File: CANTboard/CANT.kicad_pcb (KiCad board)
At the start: 2 copper layers, 67.6 x 50.8 mm, 61 parts, among them J1 Conn_02x08_Odd_Even, J2 Screw_Terminal_01x02, J3 Screw_Terminal_01x04, P1 USB, P2 SWD, SW1 SW_SPST, U1 USBLC6-2SC6, U2 SN74LVC1G14DBV, U3 ST485EBDR, U4 LD1117S33TR, U5 STM32H743VITx, U6 MCP2558FD-xSN, U7 74LVC1G66, U8 MCP2558FD-xSN, U9 74LVC1G66, Y1 Crystal

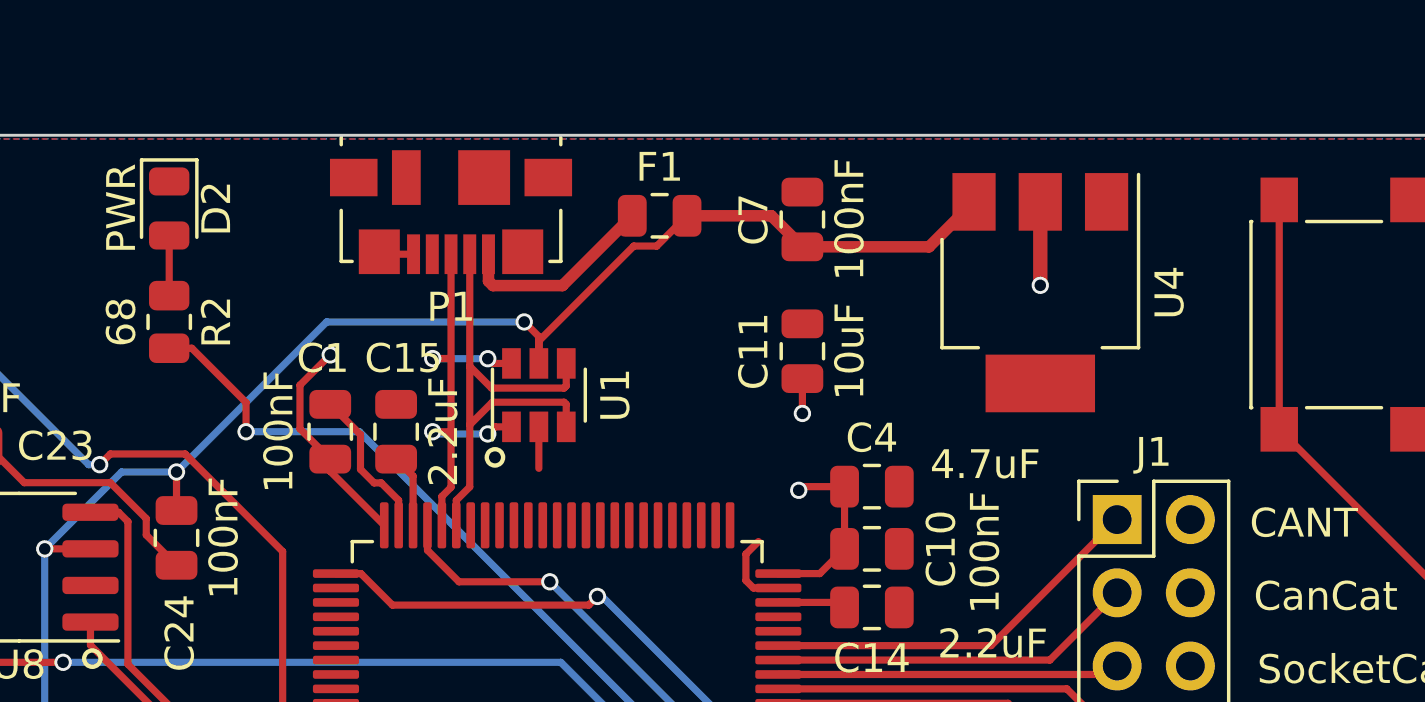
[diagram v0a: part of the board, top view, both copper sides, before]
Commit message: Switched to USB-C, in process of switching to USB-HS
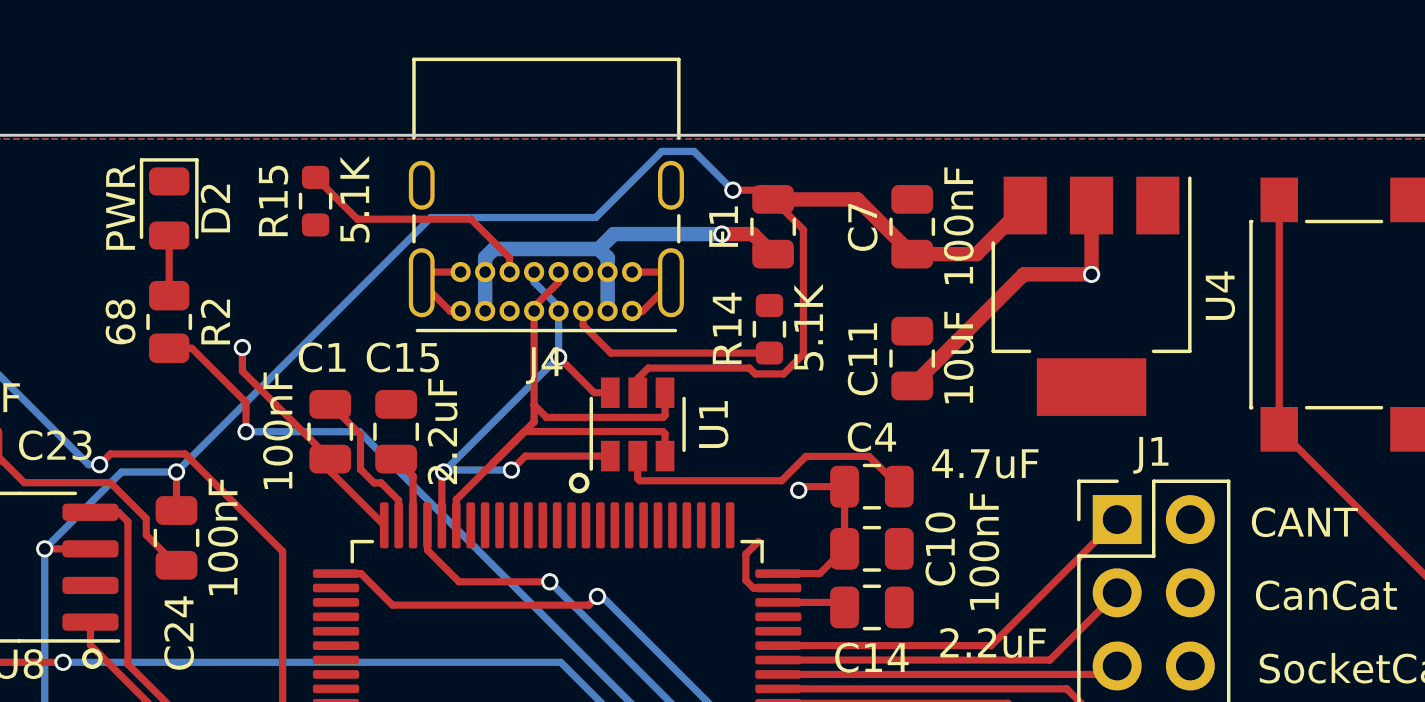
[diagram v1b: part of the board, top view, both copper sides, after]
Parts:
- removed P1: USB, Connector_USB:USB_Micro-B_Molex_47346-0001
- added J4: USB_C_Receptacle_USB2.0, Connector_USB:USB_C_Receptacle_GCT_USB4085, F.Cu at (110.3, 72.5)
- added R14: 5.1K, Resistor_SMD:R_0603_1608Metric, F.Cu at (115.1, 73.2)
- added R15: 5.1K, Resistor_SMD:R_0603_1608Metric, F.Cu at (99.3, 68.7)
- moved F1 3.96 mm to (115.2, 69.6), turned to 90 degrees
- moved C11 3.82 mm to (120.0, 74.2)
- moved C7 3.82 mm to (120.0, 69.6)
- moved U1 3.58 mm to (110.5, 76.5)
- moved U4 1.78 mm to (126.2, 72.0)
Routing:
- net GND: track 117.1 -> 131.6 mm
- net VBUS: track 85.9 -> 100.1 mm
- net Net-(J4-PadB5): track 0.00 -> 8.38 mm
- net Net-(F1-Pad1): track 6.99 -> 14.7 mm, vias 0 -> 1
- net Net-(J4-PadA5): track 0.00 -> 7.36 mm
- net VCC: track 73.8 -> 80.5 mm, vias 15 -> 14
- net /USB_DM: track 18.6 -> 23.0 mm
- net /USB_DP: track 16.5 -> 19.1 mm, vias 4 -> 3
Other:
- board text added: "5.1K"

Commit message: Everything routed, commiting before last check before ordering PCBs
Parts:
- removed P2: SWD, Connector_PinHeader_2.54mm:PinHeader_1x05_P2.54mm_Vertical
- removed Y1: Crystal, Crystal:Crystal_SMD_HC49-SD
- added  : MountingHole_3.2mm_M3, MountingHole:MountingHole_3.2mm_M3, F.Cu at (37.5, 107.3)
- added  : MountingHole_3.2mm_M3, MountingHole:MountingHole_3.2mm_M3, F.Cu at (82.5, 107.3)
- added  : MountingHole_3.2mm_M3, MountingHole:MountingHole_3.2mm_M3, F.Cu at (82.5, 65.4)
- added  : MountingHole_3.2mm_M3, MountingHole:MountingHole_3.2mm_M3, F.Cu at (28.6, 65.4)
- added C25: 100nF, Capacitor_SMD:C_0805_2012Metric, F.Cu at (31.8, 92.7)
- added C26: 1uF, Capacitor_SMD:C_0805_2012Metric, F.Cu at (24.8, 87.6)
- added C27: 1uF, Capacitor_SMD:C_0805_2012Metric, F.Cu at (34.9, 92.7)
- added C28: 100nF, Capacitor_SMD:C_0805_2012Metric, F.Cu at (29.8, 101.0)
- added C29: 100nF, Capacitor_SMD:C_0805_2012Metric, F.Cu at (27.6, 83.2)
- added P1: SWD, Connector_PinHeader_2.54mm:PinHeader_1x05_P2.54mm_Vertical, F.Cu at (66.4, 74.0)
- added R16: 20K, Resistor_SMD:R_0805_2012Metric, F.Cu at (24.8, 91.4)
- added R17: 8.06K, Resistor_SMD:R_0805_2012Metric, F.Cu at (29.2, 92.7)
- added U10: DSC1001, DSC1001:Oscillator_SMD_Microchip_DSC1001-4Pin_2.5x2.0mm, F.Cu at (29.8, 97.8)
- C1: value 100nF -> 1uF
- C11: value 10uF -> 4.7uF
- C12, C13, C14: value 2.2uF -> 100nF
- C15: value 2.2uF -> 1uF
- C16, C17: value 26pF -> 100nF
- C20: value 1uF -> 100nF
- C22, C23, C5: value 100nF -> 2.2uF
- C24: value 100nF -> 4.7uF
- C3: value 100nF -> 10uF
- C4: value 4.7uF -> 2.2uF
- J1: value Conn_02x08_Odd_Even -> USB_C_Receptacle_USB2.0; footprint Connector_PinHeader_2.54mm:PinHeader_2x08_P2.54mm_Vertical -> Connector_USB:USB_C_Receptacle_GCT_USB4085
- J2: value Screw_Terminal_01x02 -> Conn_02x08_Odd_Even; footprint TerminalBlock_Phoenix:TerminalBlock_Phoenix_PT-1,5-2-3.5-H_1x02_P3.50mm_Horizontal -> Connector_PinHeader_2.54mm:PinHeader_2x08_P2.54mm_Vertical
- J4: value USB_C_Receptacle_USB2.0 -> Screw_Terminal_01x02; footprint Connector_USB:USB_C_Receptacle_GCT_USB4085 -> TerminalBlock_Phoenix:TerminalBlock_Phoenix_PT-1,5-2-3.5-H_1x02_P3.50mm_Horizontal
- R1, R2: value 68 -> 5.1K
- R11: value 120 -> 4.7K
- R13: value 10k -> 4.7K
- R14, R15: value 5.1K -> 47; footprint Resistor_SMD:R_0603_1608Metric -> Resistor_SMD:R_0805_2012Metric
- R4, R5: value 4.7K -> 68
- R7: value 47 -> 10k
- R8: value 47 -> 120
- U1: value USBLC6-2SC6 -> USB3343; footprint Package_TO_SOT_SMD:SOT-23-6 -> Package_DFN_QFN:QFN-24-1EP_4x4mm_P0.5mm_EP2.6x2.6mm
- U2: value SN74LVC1G14DBV -> LD1117S33TR; footprint Package_TO_SOT_SMD:SOT-23-5 -> Package_TO_SOT_SMD:SOT-223
- U3: value ST485EBDR -> STM32H743VITx; footprint Package_SO:SOIC-8_3.9x4.9mm_P1.27mm -> Package_QFP:LQFP-100_14x14mm_P0.5mm
- U4: value LD1117S33TR -> MCP2558FD-xSN; footprint Package_TO_SOT_SMD:SOT-223 -> Package_SO:SOIC-8_3.9x4.9mm_P1.27mm
- U5: value STM32H743VITx -> MCP2558FD-xSN; footprint Package_QFP:LQFP-100_14x14mm_P0.5mm -> Package_SO:SOIC-8_3.9x4.9mm_P1.27mm
- U6: value MCP2558FD-xSN -> 74LVC1G66; footprint Package_SO:SOIC-8_3.9x4.9mm_P1.27mm -> Package_TO_SOT_SMD:SOT-353_SC-70-5_Handsoldering
- U8: value MCP2558FD-xSN -> SN74LVC1G14DBV; footprint Package_SO:SOIC-8_3.9x4.9mm_P1.27mm -> Package_TO_SOT_SMD:SOT-23-5
- U9: value 74LVC1G66 -> ST485EBDR; footprint Package_TO_SOT_SMD:SOT-353_SC-70-5_Handsoldering -> Package_SO:SOIC-8_3.9x4.9mm_P1.27mm
- moved SW1 117.1 mm to (22.2, 104.1), turned to 0 degrees
- moved U2 110.0 mm to (19.1, 69.8), turned to 90 degrees
- moved J1 106.2 mm to (21.0, 83.8), turned to 270 degrees
- moved R6 101.4 mm to (28.6, 105.7), turned to 270 degrees
- moved C2 98.0 mm to (25.4, 73.0), turned to 0 degrees
- moved F1 94.0 mm to (21.6, 78.1), turned to 270 degrees
- moved R13 90.4 mm to (45.1, 67.9), turned to 180 degrees
- moved C8 87.9 mm to (40.6, 87.0)
- moved C1 83.3 mm to (16.5, 78.1), turned to 270 degrees
- moved G*** 82.4 mm to (33.0, 85.7)
- moved C14 81.0 mm to (39.1, 97.8)
- moved C7 80.8 mm to (40.6, 84.5), turned to 0 degrees
- moved R14 80.5 mm to (34.5, 71.1)
- moved C3 80.3 mm to (25.4, 69.2), turned to 0 degrees
- moved U1 80.1 mm to (31.1, 87.0), turned to 180 degrees
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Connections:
- C1 pad 1: VCC -> GND
- C1 pad 2: GND -> Net-(C1-Pad2)
- C10 pad 1: VCC -> GND
- C10 pad 2: GND -> VCC
- C11 pad 1: VCC -> GND
- C11 pad 2: GND -> VCC
- C12 pad 1: Net-(C12-Pad1) -> GND
- C12 pad 2: GND -> VCC
- C13 pad 2: Net-(C13-Pad2) -> VCC
- C14 pad 1: Net-(C14-Pad1) -> GND
- C14 pad 2: GND -> VCC
- C15 pad 1: Net-(C15-Pad1) -> GND
- C15 pad 2: GND -> VCC
- C16 pad 1: GND -> VCC
- C16 pad 2: Net-(C16-Pad2) -> GND
- C17 pad 1: Net-(C17-Pad1) -> GND
- C17 pad 2: GND -> VBUS
- C18 pad 1: GND -> VCC
- C18 pad 2: /NRST -> GND
- C19 pad 2: VCC -> VBUS
- C2 pad 1: GND -> VBUS
- C2 pad 2: VCC -> GND
- C22 pad 1: GND -> Net-(C22-Pad1)
- C22 pad 2: VBUS -> GND
- C23 pad 2: VCC -> Net-(C23-Pad2)
- C4 pad 1: VCC -> Net-(C4-Pad1)
- C5 pad 1: VCC -> Net-(C5-Pad1)
- C6 pad 1: VCC -> GND
- C6 pad 2: GND -> /Microcontroller/NRST
- C7 pad 1: VBUS -> GND
- C7 pad 2: GND -> VCC
- C8 pad 1: VCC -> GND
- C8 pad 2: GND -> VCC
- C9 pad 1: VCC -> GND
- C9 pad 2: GND -> VCC
- F1 pad 1: Net-(F1-Pad1) -> VBUS
- F1 pad 2: VBUS -> Net-(F1-Pad2)
- J2 pad 2: Net-(J2-Pad2) -> VCC
- J3 pad 1: CAN1_L -> CAN3_L
- J3 pad 2: CAN1_H -> CAN3_H
- J3 pad 3: CAN2_L -> CAN1_L
- J3 pad 4: CAN2_H -> CAN1_H
- JP1 pad 1: Net-(JP1-Pad1) -> (no net)
- JP1 pad 2: CAN2_L -> BOOT0
- JP1 pad 3: Net-(JP1-Pad3) -> VCC
- JP2 pad 1: Net-(JP2-Pad1) -> (no net)
- JP2 pad 2: CAN1_L -> CAN3_L
- JP3 pad 1: Net-(JP3-Pad1) -> (no net)
- JP3 pad 2: BOOT0 -> CAN1_L
- JP3 pad 3: VCC -> Net-(JP3-Pad3)
- R1 pad 1: Net-(D1-Pad2) -> GND
- R1 pad 2: LED_ACT1 -> Net-(J1-PadA5)
- R10 pad 1: CAN2_SHORT -> CAN3_SHORT
- R11 pad 1: Net-(JP2-Pad3) -> CAN1_SHORT
- R11 pad 2: CAN1_H -> GND
- R12 pad 1: CAN1_SHORT -> Net-(C22-Pad1)
- R13 pad 1: BOOT0 -> VBUS
- R13 pad 2: GND -> Net-(C23-Pad2)
- R14 pad 1: Net-(J4-PadA5) -> Net-(C22-Pad1)
- R14 pad 2: GND -> Net-(J4-Pad2)
- R15 pad 1: GND -> Net-(C23-Pad2)
- R15 pad 2: Net-(J4-PadB5) -> Net-(J4-Pad1)
- R2 pad 1: Net-(D2-Pad2) -> GND
- R2 pad 2: LED_PWR1 -> Net-(J1-PadB5)
- R3 pad 1: Net-(D3-Pad2) -> Net-(D1-Pad2)
- R3 pad 2: LED_ACT2 -> LED_ACT1
- R4 pad 1: Net-(C12-Pad1) -> Net-(D2-Pad2)
- R4 pad 2: GND -> LED_PWR1
- R5 pad 1: VBUS -> Net-(D3-Pad2)
- R5 pad 2: Net-(C13-Pad2) -> LED_ACT2
- R6 pad 2: /NRST -> /Microcontroller/NRST
- R7 pad 1: Net-(C12-Pad1) -> BOOT0
- R7 pad 2: Net-(J2-Pad2) -> GND
- R8 pad 1: Net-(C13-Pad2) -> Net-(JP2-Pad3)
- R8 pad 2: Net-(J2-Pad1) -> CAN3_H
- R9 pad 1: Net-(JP1-Pad3) -> Net-(JP3-Pad3)
- R9 pad 2: CAN2_H -> CAN1_H
- SW1 pad 2: /NRST -> /Microcontroller/NRST
- U1 pad 1: /USB_DP -> USB_DIR
- U1 pad 2: GND -> USB_CK
- U1 pad 3: /USB_DM -> USB_NXT
- U1 pad 4: /USB_DM -> USB_D0
- U1 pad 5: VBUS -> USB_D1
- U1 pad 6: /USB_DP -> USB_D2
- U2 pad 1: Net-(U2-Pad1) -> GND
- U2 pad 2: J1708_TX -> VCC
- U2 pad 3: GND -> VBUS
- U2 pad 4: Net-(U2-Pad4) -> (no net)
- U3 pad 1: J1708_RX -> (no net)
- U3 pad 2: GND -> (no net)
- U3 pad 3: Net-(U2-Pad4) -> (no net)
- U3 pad 4: GND -> (no net)
- U3 pad 5: GND -> (no net)
- U3 pad 6: Net-(C13-Pad2) -> VCC
- U3 pad 7: Net-(C12-Pad1) -> (no net)
- U3 pad 8: VCC -> (no net)
- U4 pad 1: GND -> CAN3_TX
- U4 pad 2: VCC -> GND
- U4 pad 4: (no net) -> CAN3_RX
- U5 pad 1: Net-(U5-Pad1) -> CAN1_TX
- U5 pad 2: Net-(U5-Pad2) -> GND
- U5 pad 3: Net-(U5-Pad3) -> VBUS
- U5 pad 4: Net-(U5-Pad4) -> CAN1_RX
- U5 pad 5: Net-(U5-Pad5) -> VCC
- U5 pad 6: VCC -> CAN1_L
- U5 pad 7: Net-(U5-Pad7) -> CAN1_H
- U5 pad 8: Net-(U5-Pad8) -> GND
- U6 pad 1: CAN2_TX -> CAN3_L
- U6 pad 2: GND -> CAN3_H
- U6 pad 3: VBUS -> GND
- U6 pad 4: CAN2_RX -> CAN3_SHORT
- U7 pad 1: CAN2_L -> CAN1_L
- U7 pad 2: CAN2_H -> CAN1_H
- U7 pad 4: CAN2_SHORT -> CAN1_SHORT
- U8 pad 1: CAN1_TX -> (no net)
- U8 pad 2: GND -> J1708_TX
- U8 pad 3: VBUS -> GND
- U8 pad 4: CAN1_RX -> Net-(U8-Pad4)
- U9 pad 1: CAN1_L -> J1708_RX
- U9 pad 2: CAN1_H -> GND
- U9 pad 3: GND -> Net-(U8-Pad4)
- U9 pad 4: CAN1_SHORT -> GND
- U9 pad 5: VCC -> GND
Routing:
- net /NRST: track 99.4 -> 0.00 mm, vias 1 -> 0
- net /Microcontroller/NRST: track 0.00 -> 80.9 mm, vias 0 -> 4
- net /SWDIO: track 48.1 -> 0.00 mm, vias 1 -> 0
- net /SWCLK: track 47.9 -> 0.00 mm, vias 1 -> 0
- net CAN3_H: track 0.00 -> 47.7 mm
- net CAN2_L: track 39.8 -> 0.00 mm, vias 2 -> 0
- net USB_D7: track 0.00 -> 38.6 mm, vias 0 -> 2
- net CAN3_SHORT: track 0.00 -> 38.6 mm, vias 0 -> 2
- net USB_D6: track 0.00 -> 36.8 mm, vias 0 -> 2
- net USB_STP: track 0.00 -> 36.4 mm, vias 0 -> 2
- net USB_D5: track 0.00 -> 36.1 mm, vias 0 -> 2
- net CAN2_SHORT: track 35.7 -> 0.00 mm, vias 2 -> 0
- net USB_D2: track 0.00 -> 35.7 mm, vias 0 -> 2
- net USB_D3: track 0.00 -> 35.6 mm, vias 0 -> 2
- net USB_DIR: track 0.00 -> 35.5 mm, vias 0 -> 2
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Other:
- board size 67.6 x 50.8 mm -> 82 x 49.1 mm
- copper layers 2 -> 4
- board text added: "1. CanCat 2. CANT 3. SocketCan 4. TruckDevil"
- board text added: "8 7 6 5 4 3 2 1"
- board text added: "CAN 1 - +"
- board text added: "CAN 2 - +"
- board text added: "RST"
- board text added: "SWCLK"
- board text added: "SWDIO"
- board text added: "Term"
- board text removed: "100K"
- board text removed: "100nF"
- board text removed: "10K"
- board text removed: "10uF"
- board text removed: "120"
- board text removed: "1uF"
- board text removed: "2.2uF"
- board text removed: "26pF"
- board text removed: "4.7K"
- board text removed: "4.7uF"
- board text removed: "47"
- board text removed: "5.1K"
- board text removed: "68"
- board text removed: "CAN1"
- board text removed: "CAN2"
- board text removed: "CANT"
- board text removed: "CLK"
- board text removed: "CanCat"
- board text removed: "DIO"
- board text removed: "HI"
- board text removed: "J1708"
- board text removed: "LO"
- board text removed: "NRST"
- board text removed: "PWR"
- board text removed: "Prog1"
- board text removed: "Prog2"
- board text removed: "Prog3"
- board text removed: "Prog4"
- board text removed: "SWD"
- board text removed: "SocketCan"
- board text removed: "TERM"
- board text removed: "TruckDevil"

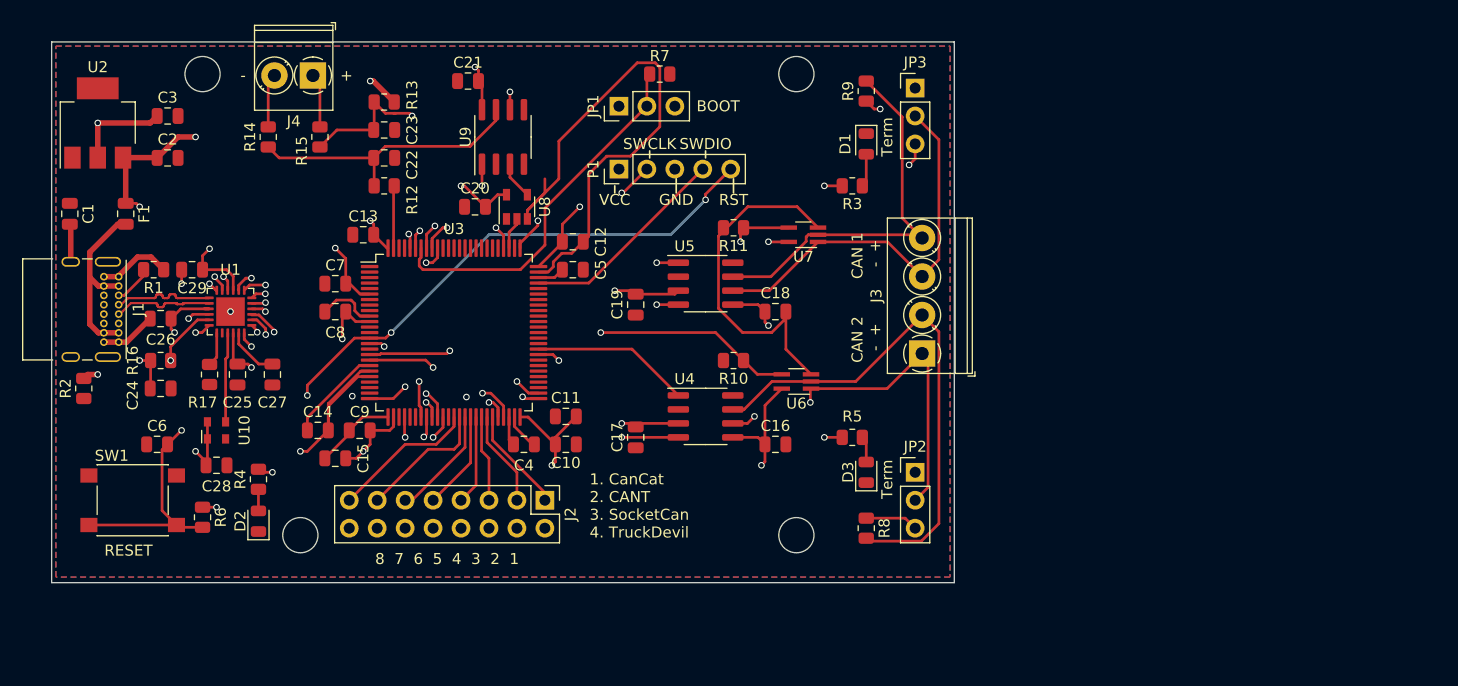
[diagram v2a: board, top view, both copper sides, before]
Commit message: Final review, ordering v0.1 PCB off this design
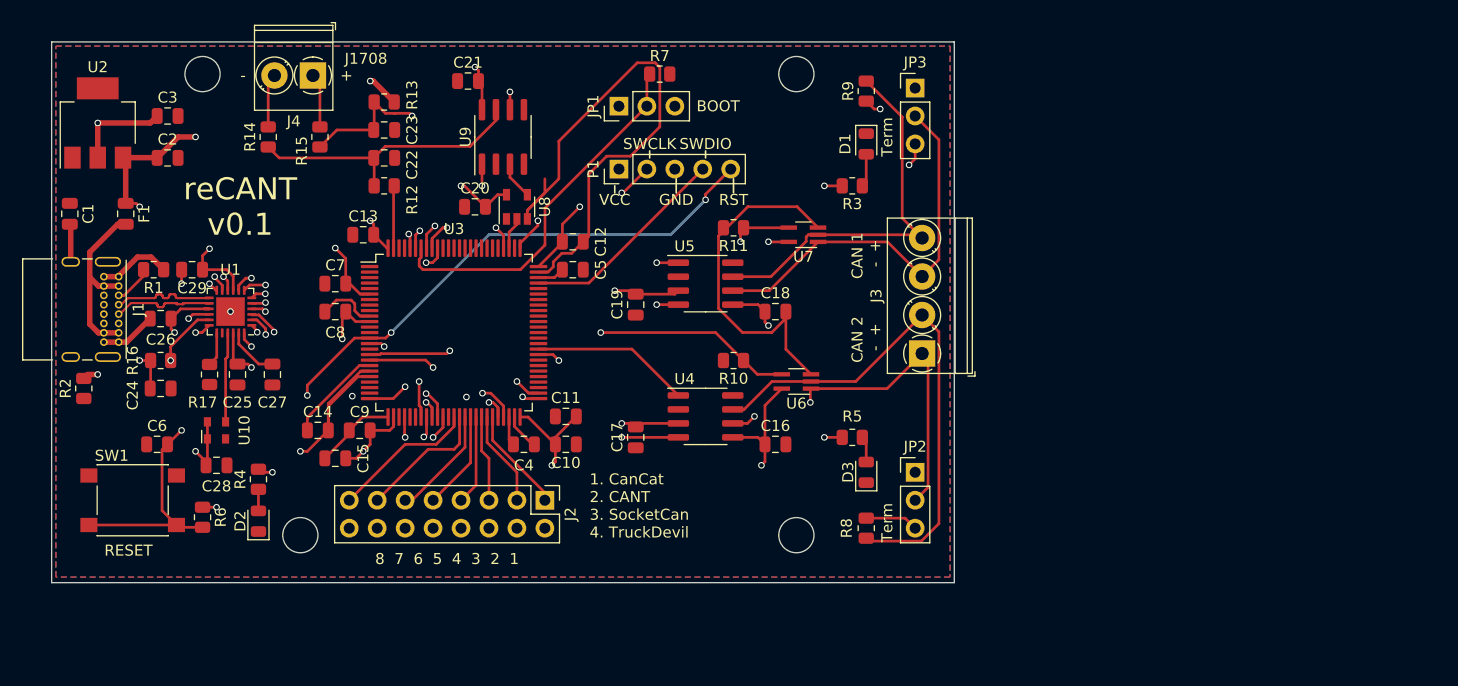
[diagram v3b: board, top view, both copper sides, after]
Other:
- board text added: "J1708"
- board text added: "reCANT v0.1"
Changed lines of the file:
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@@
   (general
     (thickness 1.6)
-    (drawings 25)
+    (drawings 27)
     (tracks 3009)
     (zones 0)
@@
     (tags resistor)
     (attr smd)
-    (fp_text reference R8 (at 0 -1.65 90) (layer F.SilkS)
+    (fp_text reference R8 (at 0 1.778 90) (layer F.SilkS)
       (effects (font (size 1 1) (thickness 0.15)))
     )
@@
     )
   )
+  (gr_text J1708 (at 43.434 64.008) (layer F.SilkS)
+    (effects (font (size 1 1) (thickness 0.15)))
+  )
+  (gr_text "reCANT\nv0.1" (at 32.004 77.47) (layer F.SilkS)
+    (effects (font (size 2 2) (thickness 0.3)))
+  )
   (gr_text "1. CanCat\n2. CANT\n3. SocketCan\n4. TruckDevil" (at 63.754 104.648) (layer F.SilkS)
     (effects (font (size 1 1) (thickness 0.15)) (justify left))
@@
     (effects (font (size 1 1) (thickness 0.15)))
   )
-  (gr_text "Term\n" (at 90.805 102.235 90) (layer F.SilkS)
+  (gr_text "Term\n" (at 90.805 106.172 90) (layer F.SilkS)
     (effects (font (size 1 1) (thickness 0.15)))
   )
